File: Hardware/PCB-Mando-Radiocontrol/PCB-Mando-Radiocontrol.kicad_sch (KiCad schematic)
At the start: 25 parts, among them J2 ALIMENTACION, J3 USB 2.0 a UART TTL 6 pines CP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, SW1 SW_SPDT, U1 ATMEGA328P, U2 Nrf24l01, U3 AMS1117-3.3, U4 AMS1117-5.0, U5 COM-09032, U6 COM-09032, Y1 16MHZ

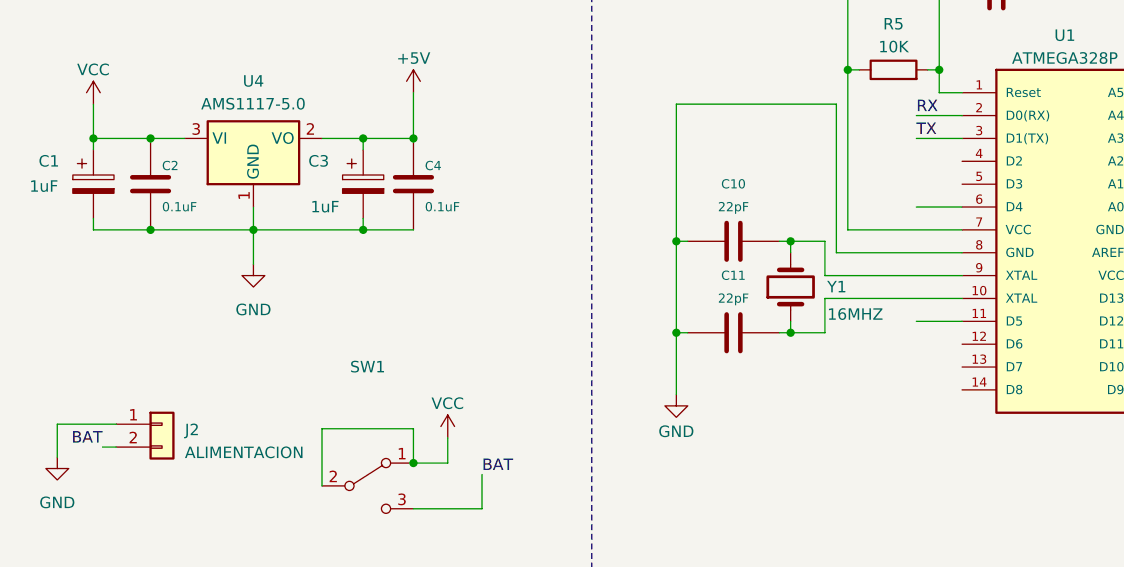
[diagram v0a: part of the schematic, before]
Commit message: aplique sugerencias de markow y mias, agregue botones modifique esquematico y pcb
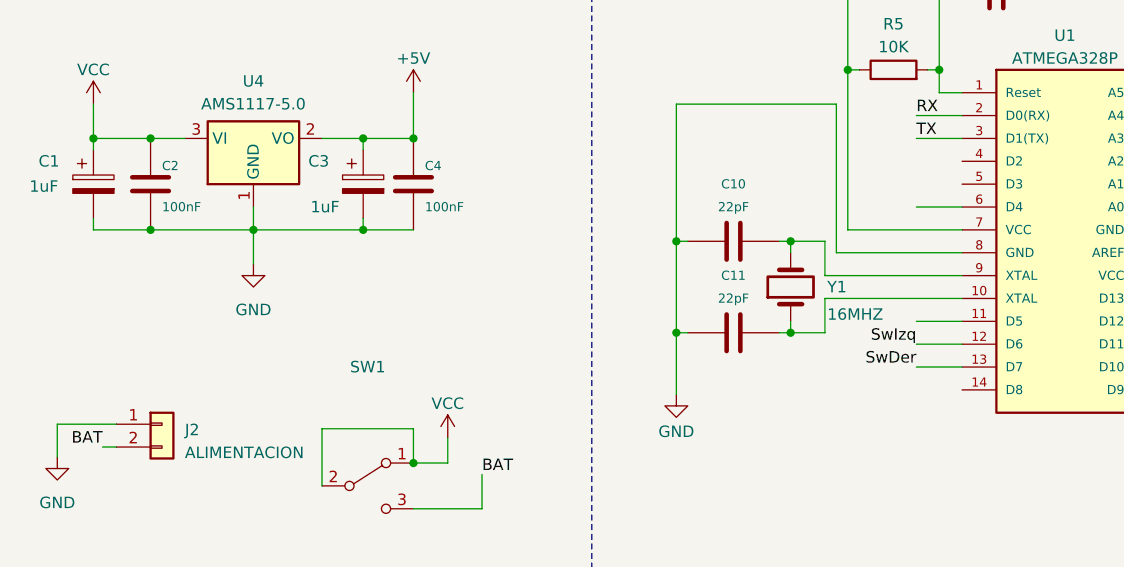
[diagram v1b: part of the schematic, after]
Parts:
- C2, C4: value 0.1uF -> 100nF
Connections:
- net SwDer: now also U1.13 (D7)
- net SwIzq: now also U1.12 (D6)

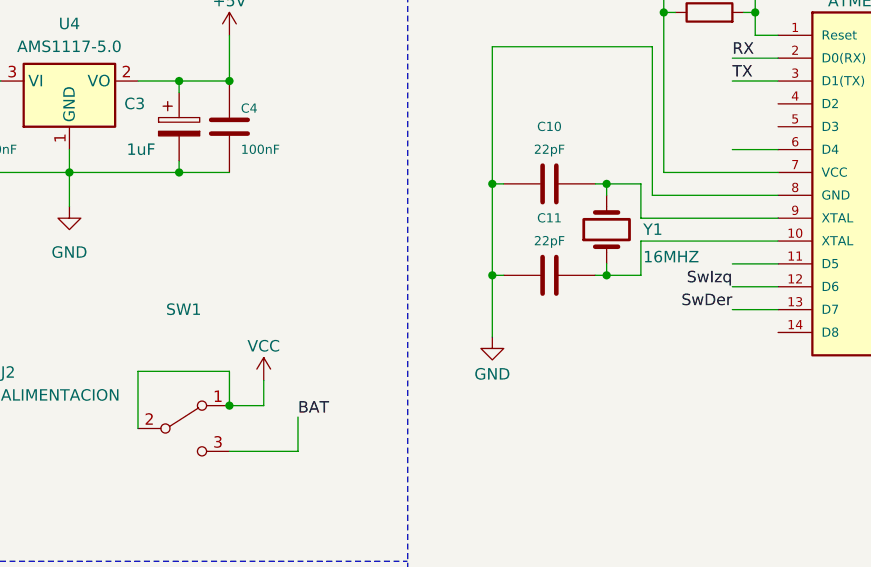
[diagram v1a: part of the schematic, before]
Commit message: Ordene serigrafia y cambie los capacitores c11 y c12 tht por cmd
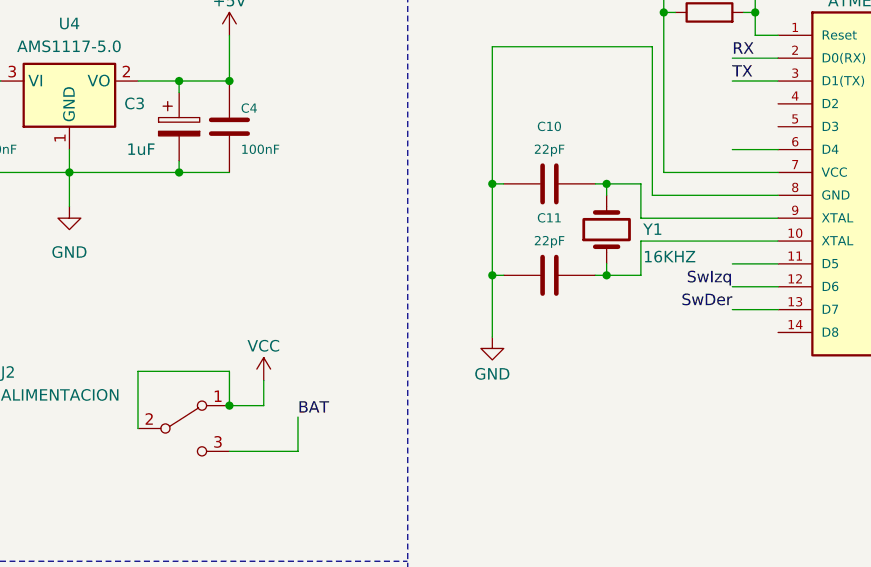
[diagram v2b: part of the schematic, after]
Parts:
- C10, C11: footprint Capacitor_THT:C_Disc_D3.0mm_W1.6mm_P2.50mm -> Capacitor_SMD:C_1206_3216Metric
- SW1: value SW_SPDT -> ~
- Y1: value 16MHZ -> 16KHZ
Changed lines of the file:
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@@
       (effects (font (size 1.27 1.27)) (justify right))
     )
-    (property "Value" "16MHZ" (at 106.934 93.218 90)
+    (property "Value" "16KHZ" (at 106.934 93.218 90)
       (effects (font (size 1.27 1.27)) (justify right))
     )
@@
     (in_bom yes) (on_board yes) (dnp no)
     (property "Reference" "SW1" (at 55.88 99.06 0)
-      (effects (font (size 1.27 1.27)))
-    )
-    (property "Value" "SW_SPDT" (at 55.88 117.348 0)
+      (effects (font (size 1.27 1.27)) hide)
+    )
+    (property "Value" "~" (at 55.88 117.348 0)
       (effects (font (size 1.27 1.27)) hide)
     )
@@
       (effects (font (size 1.016 1.016)))
     )
-    (property "Footprint" "Capacitor_THT:C_Disc_D3.0mm_W1.6mm_P2.50mm" (at 100.33 94.2848 0)
+    (property "Footprint" "Capacitor_SMD:C_1206_3216Metric" (at 100.33 94.2848 0)
       (effects (font (size 0.762 0.762)) hide)
     )
@@
       (effects (font (size 1.016 1.016)))
     )
-    (property "Footprint" "Capacitor_THT:C_Disc_D3.0mm_W1.6mm_P2.50mm" (at 100.33 84.1248 0)
+    (property "Footprint" "Capacitor_SMD:C_1206_3216Metric" (at 100.33 84.1248 0)
       (effects (font (size 0.762 0.762)) hide)
     )

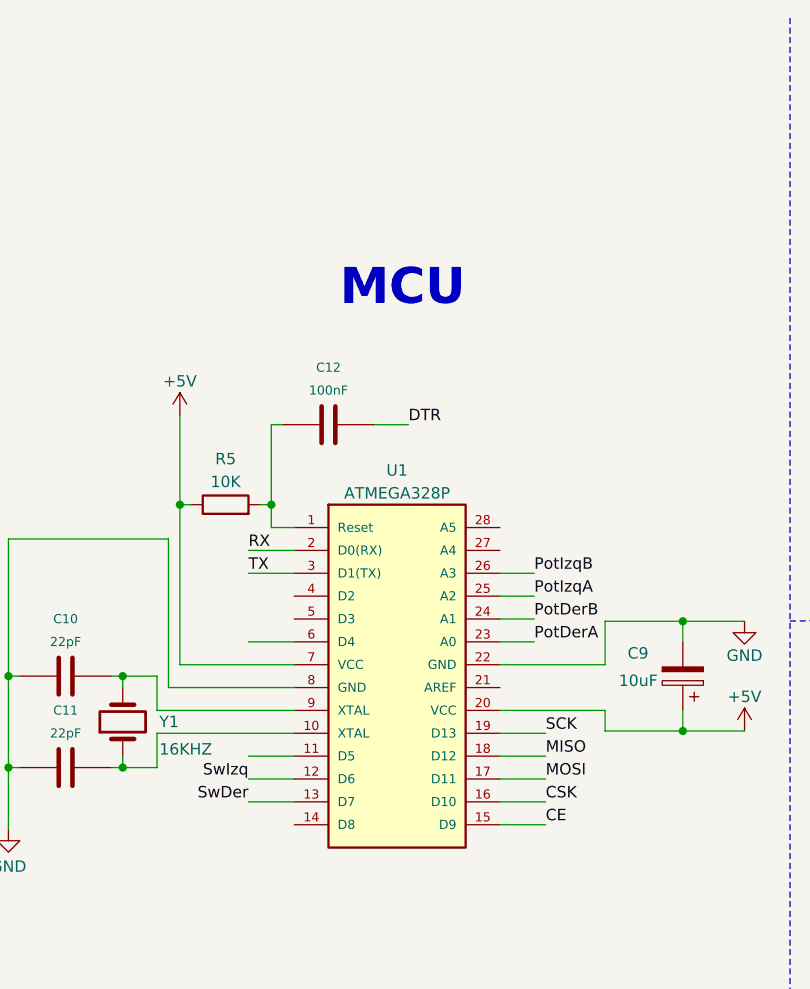
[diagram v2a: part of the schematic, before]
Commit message: Agregue LED y BUZZER , pcb listo para montar
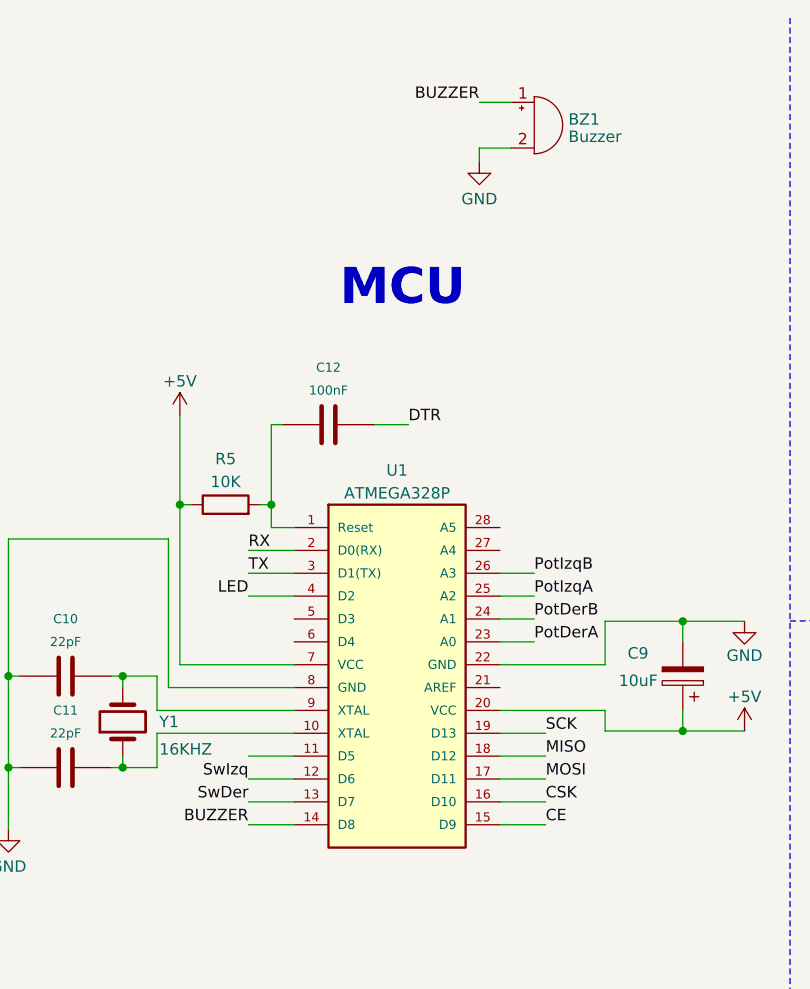
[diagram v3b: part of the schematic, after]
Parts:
- added BZ1: Buzzer, EESTN5:Buzzer_12mm, symbol EESTN5:Buzzer
- J2: footprint Connector_JST:JST_EH_S2B-EH_1x02_P2.50mm_Horizontal -> Connector_JST:JST_PH_B2B-PH-K_1x02_P2.00mm_Vertical
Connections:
- net GND: now also BZ1.2 (+)
- net BUZZER: now reaches U1.14 (D8)
- net BUZZER: now also BZ1.1 (-)
- net LED: now reaches U1.4 (D2)
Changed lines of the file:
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@@
   (junction (at 31.75 36.83) (diameter 0) (color 0 0 0 0)
   )
+  (wire (pts (xy 142.494 21.336) (xy 146.05 21.336))
+    (stroke (width 0) (type default))
+  )
   (wire (pts (xy 212.09 107.95) (xy 218.44 107.95))
     (stroke (width 0) (type default))
@@
     (stroke (width 0) (type default))
   )
+  (wire (pts (xy 116.84 101.6) (xy 121.92 101.6))
+    (stroke (width 0) (type default))
+  )
   (wire (pts (xy 144.78 76.2) (xy 148.59 76.2))
     (stroke (width 0) (type default))
@@
     (stroke (width 0) (type dash))
   )
-  (wire (pts (xy 116.84 81.28) (xy 121.92 81.28))
-    (stroke (width 0) (type default))
-  )
   (wire (pts (xy 212.09 113.03) (xy 218.44 113.03))
     (stroke (width 0) (type default))
@@
     (stroke (width 0) (type default))
   )
+  (wire (pts (xy 146.05 26.416) (xy 142.494 26.416))
+    (stroke (width 0) (type default))
+  )
   (wire (pts (xy 237.49 39.37) (xy 247.65 39.37))
     (stroke (width 0) (type default))
@@
     (stroke (width 0) (type default))
   )
+  (wire (pts (xy 116.84 76.2) (xy 121.92 76.2))
+    (stroke (width 0) (type default))
+  )
   (wire (pts (xy 33.02 146.05) (xy 33.02 147.32))
     (stroke (width 0) (type default))
@@
     (stroke (width 0) (type default))
   )
+  (wire (pts (xy 142.494 26.416) (xy 142.494 27.94))
+    (stroke (width 0) (type default))
+  )
   (wire (pts (xy 60.96 105.918) (xy 60.96 109.728))
     (stroke (width 0) (type default))
@@
     (effects (font (size 1.27 1.27)) (justify left bottom))
   )
+  (label "BUZZER" (at 142.494 21.336 180) (fields_autoplaced)
+    (effects (font (size 1.27 1.27)) (justify right bottom))
+  )
   (label "DTR" (at 134.62 57.15 0) (fields_autoplaced)
     (effects (font (size 1.27 1.27)) (justify left bottom))
@@
     (effects (font (size 1.27 1.27)) (justify left bottom))
   )
+  (label "LED" (at 116.84 76.2 180) (fields_autoplaced)
+    (effects (font (size 1.27 1.27)) (justify right bottom))
+  )
   (label "CE" (at 212.09 102.87 0) (fields_autoplaced)
     (effects (font (size 1.27 1.27)) (justify left bottom))
   )
+  (label "BUZZER" (at 116.84 101.6 180) (fields_autoplaced)
+    (effects (font (size 1.27 1.27)) (justify right bottom))
+  )
   (label "PotDerB" (at 247.65 34.29 180) (fields_autoplaced)
     (effects (font (size 1.27 1.27)) (justify right bottom))
@@
     )
   )
+  (symbol (lib_id "EESTN5:Buzzer") (at 148.59 23.876 0) (unit 1)
+    (in_bom yes) (on_board yes) (dnp no) (fields_autoplaced)
+    (property "Reference" "BZ1" (at 152.3862 23.2323 0)
+      (effects (font (size 1.27 1.27)) (justify left))
+    )
+    (property "Value" "Buzzer" (at 152.3862 25.1533 0)
+      (effects (font (size 1.27 1.27)) (justify left))
+    )
+    (property "Footprint" "EESTN5:Buzzer_12mm" (at 147.955 21.336 90)
+      (effects (font (size 1.27 1.27)) hide)
+    )
+    (property "Datasheet" "" (at 147.955 21.336 90)
+      (effects (font (size 1.27 1.27)) hide)
+    )
+    (pin "1")
+    (pin "2")
+    (instances
+      (project "PCB-Mando-Radiocontrol"
+        (path "/a09d701e-8048-4e72-8e3a-cb0f8f921380"
+          (reference "BZ1") (unit 1)
+        )
+      )
+    )
+  )
   (symbol (lib_id "power:+3V3") (at 60.96 31.75 0) (unit 1)
     (in_bom yes) (on_board yes) (dnp no) (fields_autoplaced)
@@
       (effects (font (size 1.27 1.27)) (justify left))
     )
-    (property "Footprint" "Connector_JST:JST_EH_S2B-EH_1x02_P2.50mm_Horizontal" (at 33.02 105.41 0)
+    (property "Footprint" "Connector_JST:JST_PH_B2B-PH-K_1x02_P2.00mm_Vertical" (at 33.02 105.41 0)
       (effects (font (size 1.27 1.27)) hide)
     )
@@
         )
       )
+    )
+  )
+  (symbol (lib_id "power:GND") (at 142.494 27.94 0) (unit 1)
+    (in_bom yes) (on_board yes) (dnp no) (fields_autoplaced)
+    (property "Reference" "#PWR031" (at 142.494 34.29 0)
+      (effects (font (size 1.27 1.27)) hide)
+    )
+    (property "Value" "GND" (at 142.494 32.0755 0)
+      (effects (font (size 1.27 1.27)))
+    )
+    (property "Footprint" "" (at 142.494 27.94 0)
+      (effects (font (size 1.27 1.27)) hide)
+    )
+    (property "Datasheet" "" (at 142.494 27.94 0)
+      (effects (font (size 1.27 1.27)) hide)
+    )
+    (pin "1")
+    (instances
+      (project "PCB-Mando-Radiocontrol"
+        (path "/a09d701e-8048-4e72-8e3a-cb0f8f921380"
+          (reference "#PWR031") (unit 1)
+        )
+      )

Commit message: prueba de transmisor y receptor one
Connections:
- net CSK renamed CSN
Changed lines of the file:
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@@
     (effects (font (size 1.27 1.27)) (justify right bottom))
   )
-  (label "CSK" (at 149.86 99.06 0) (fields_autoplaced)
+  (label "CSN" (at 149.86 99.06 0) (fields_autoplaced)
     (effects (font (size 1.27 1.27)) (justify left bottom))
   )
@@
     (effects (font (size 1.27 1.27)) (justify left bottom))
   )
-  (label "CSK" (at 212.09 105.41 0) (fields_autoplaced)
+  (label "CSN" (at 212.09 105.41 0) (fields_autoplaced)
     (effects (font (size 1.27 1.27)) (justify left bottom))
   )
